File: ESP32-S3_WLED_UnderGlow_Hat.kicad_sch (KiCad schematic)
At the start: 0 parts

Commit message: Update ESP32-S3_WLED_UnderGlow_Hat.kicad_sch
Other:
- title: ESP32-S3_IOHat -> ESP32-S3 WLED UnderGlow Hat
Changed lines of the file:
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@@
 	(paper "A4")
 	(title_block
-		(title "ESP32-S3_IOHat")
+		(title "ESP32-S3 WLED UnderGlow Hat")
 		(date "2026-01-03")
 		(rev "C")

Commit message: Updated Net Names for FSPI and I2S nets
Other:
- sheet IO_Board ports: added FSPI_{CLK}, FSPI_{HD}, FSPI_{MISO}, FSPI_{MOSI}, FSPI_{WP}, I^{2}S_{MCLK}, I^{2}S_{SCK}, I^{2}S_{SD}, I^{2}S_{WS}, ~{FSPI_{CS0}}; removed FSPIHD, FSPIWP, MCLK, MISO, MOSI, SCK, SCLK, SD, WS, ~{FSPICS}
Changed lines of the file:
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@@
 			)
 		)
-		(pin "FSPIHD" bidirectional
+		(pin "FSPI_{HD}" bidirectional
 			(at 109.22 91.44 90)
 			(effects
@@
 			)
 		)
-		(pin "~{FSPICS}" bidirectional
+		(pin "~{FSPI_{CS0}}" bidirectional
 			(at 111.76 91.44 90)
 			(effects
@@
 			)
 		)
-		(pin "MOSI" bidirectional
+		(pin "FSPI_{MOSI}" bidirectional
 			(at 114.3 91.44 90)
 			(effects
@@
 			)
 		)
-		(pin "SCLK" bidirectional
+		(pin "FSPI_{CLK}" bidirectional
 			(at 116.84 91.44 90)
 			(effects
@@
 			)
 		)
-		(pin "MISO" bidirectional
+		(pin "FSPI_{MISO}" bidirectional
 			(at 119.38 91.44 90)
 			(effects
@@
 			)
 		)
-		(pin "FSPIWP" bidirectional
+		(pin "FSPI_{WP}" bidirectional
 			(at 121.92 91.44 90)
 			(effects
@@
 			)
 		)
-		(pin "SD" bidirectional
+		(pin "I^{2}S_{SD}" bidirectional
 			(at 137.16 91.44 90)
 			(effects
@@
 			)
 		)
-		(pin "MCLK" bidirectional
+		(pin "I^{2}S_{MCLK}" bidirectional
 			(at 142.24 91.44 90)
 			(effects
@@
 			)
 		)
-		(pin "SCK" bidirectional
+		(pin "I^{2}S_{SCK}" bidirectional
 			(at 165.1 91.44 90)
 			(effects
@@
 			)
 		)
-		(pin "WS" bidirectional
+		(pin "I^{2}S_{WS}" bidirectional
 			(at 167.64 91.44 90)
 			(effects

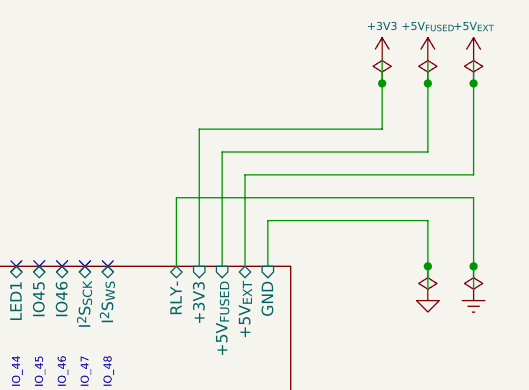
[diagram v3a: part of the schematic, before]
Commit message: schematic updated with new ESP32-S3_D1_Pico symbol
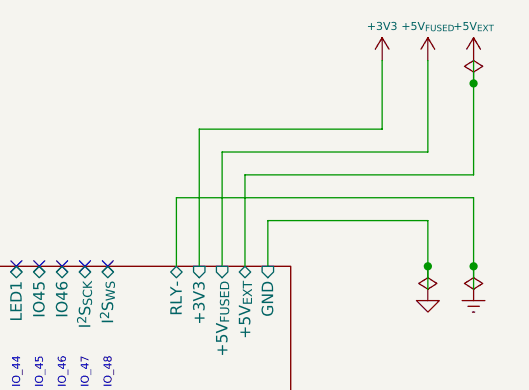
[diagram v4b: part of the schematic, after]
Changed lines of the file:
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@@
-	)
-	(junction
-		(at 198.12 71.12)
-		(diameter 0)
-		(color 0 0 0 0)
 	)
 	(junction
@@
 		(color 0 0 0 0)
 	)
-	(junction
-		(at 203.2 71.12)
-		(diameter 0)
-		(color 0 0 0 0)
-	)
 	(no_connect
 		(at 119.38 91.44)
@@
 	(wire
 		(pts
-			(xy 203.2 68.58) (xy 203.2 71.12)
-		)
-		(stroke
-			(width 0)
-			(type default)
-		)
-	)
-	(wire
-		(pts
 			(xy 180.34 78.74) (xy 203.2 78.74)
 		)
@@
 	(wire
 		(pts
-			(xy 198.12 71.12) (xy 198.12 76.2)
+			(xy 198.12 68.58) (xy 198.12 76.2)
 		)
 		(stroke
@@
 	(wire
 		(pts
-			(xy 203.2 71.12) (xy 203.2 78.74)
+			(xy 203.2 68.58) (xy 203.2 78.74)
 		)
 		(stroke
@@
 		(pts
 			(xy 175.26 83.82) (xy 208.28 83.82)
-		)
-		(stroke
-			(width 0)
-			(type default)
-		)
-	)
-	(wire
-		(pts
-			(xy 198.12 68.58) (xy 198.12 71.12)
 		)
 		(stroke
@@
 	(symbol
 		(lib_id "power:PWR_FLAG")
-		(at 203.2 71.12 0)
-		(unit 1)
-		(exclude_from_sim no)
-		(in_bom yes)
-		(on_board yes)
-		(dnp no)
-		(fields_autoplaced yes)
-		(property "Reference" "#FLG01"
-			(at 203.2 69.215 0)
-			(effects
-				(font
-					(size 0.889 0.889)
-				)
-				(hide yes)
-			)
-		)
-		(property "Value" "+5V_{FUSED}"
-			(at 203.2 66.04 0)
-			(effects
-				(font
-					(size 0.889 0.889)
-				)
-				(hide yes)
-			)
-		)
-		(property "Footprint" ""
-			(at 203.2 71.12 0)
-			(effects
-				(font
-					(size 1.27 1.27)
-				)
-				(hide yes)
-			)
-		)
-		(property "Datasheet" "~"
-			(at 203.2 71.12 0)
-			(effects
-				(font
-					(size 1.27 1.27)
-				)
-				(hide yes)
-			)
-		)
-		(property "Description" "Special symbol for telling ERC where power comes from"
-			(at 203.2 71.12 0)
-			(effects
-				(font
-					(size 1.27 1.27)
-				)
-				(hide yes)
-			)
-		)
-		(pin "1"
-		)
-		(instances
-			(project "ESP32-S3_WLED_UnderGlow_Hat"
-				(path "/67f7b1e1-e87f-421a-8424-bb26889ab157"
-					(reference "#FLG01")
-					(unit 1)
-				)
-			)
-		)
-	)
-	(symbol
-		(lib_id "power:PWR_FLAG")
 		(at 208.28 71.12 0)
 		(unit 1)
@@
 					(unit 1)
 				)
-			)
-		)
-	)
-	(symbol
-		(lib_id "power:PWR_FLAG")
-		(at 198.12 71.12 0)
-		(unit 1)
-		(exclude_from_sim no)
-		(in_bom yes)
-		(on_board yes)
-		(dnp no)
-		(fields_autoplaced yes)
-		(property "Reference" "#FLG0103"
-			(at 198.12 69.215 0)
-			(effects
-				(font
-					(size 0.889 0.889)
-				)
-				(hide yes)
-			)
-		)
-		(property "Value" "+3V3"
-			(at 198.12 66.04 0)
-			(effects
-				(font
-					(size 0.889 0.889)
-				)
-				(hide yes)
-			)
-		)
-		(property "Footprint" ""
-			(at 198.12 71.12 0)
-			(effects
-				(font
-					(size 1.27 1.27)
-				)
-				(hide yes)
-			)
-		)
-		(property "Datasheet" "~"
-			(at 198.12 71.12 0)
-			(effects
-				(font
-					(size 1.27 1.27)
-				)
-				(hide yes)
-			)
-		)
-		(property "Description" "Special symbol for telling ERC where power comes from"
-			(at 198.12 71.12 0)
-			(effects
-				(font
-					(size 1.27 1.27)
-				)
-				(hide yes)
-			)
-		)
-		(pin "1"
-		)
-		(instances
-			(project "ESP32-S3_WLED_UnderGlow_Hat"
-				(path "/67f7b1e1-e87f-421a-8424-bb26889ab157"
-					(reference "#FLG0103")
-					(unit 1)
-				)

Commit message: JLCPCB: W2026061412450502 2026-06-14 PCB: Y62-5297522A PCBA: SMT026061460215-5297522A
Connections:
- no-connect marks 32 -> 27
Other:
- sheet IO_Board ports: added none; removed +5V_{EXT}, IO00, IO01, IO03, IO45, IO46
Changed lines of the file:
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@@
 		(color 0 0 0 0)
 	)
-	(junction
-		(at 208.28 71.12)
-		(diameter 0)
-		(color 0 0 0 0)
-	)
 	(no_connect
 		(at 119.38 91.44)
@@
 	)
 	(no_connect
-		(at 81.28 101.6)
-	)
-	(no_connect
 		(at 114.3 91.44)
 	)
@@
 	)
 	(no_connect
-		(at 81.28 106.68)
-	)
-	(no_connect
 		(at 129.54 91.44)
 	)
@@
 	)
 	(no_connect
-		(at 162.56 91.44)
-	)
-	(no_connect
 		(at 127 91.44)
 	)
@@
 	)
 	(no_connect
-		(at 160.02 91.44)
-	)
-	(no_connect
 		(at 157.48 91.44)
 	)
@@
 		(at 134.62 91.44)
 	)
-	(no_connect
-		(at 81.28 109.22)
-	)
-	(wire
-		(pts
-			(xy 208.28 71.12) (xy 208.28 81.28)
-		)
-		(stroke
-			(width 0)
-			(type default)
-		)
-	)
 	(wire
 		(pts
@@
 	(wire
 		(pts
-			(xy 182.88 81.28) (xy 182.88 91.44)
-		)
-		(stroke
-			(width 0)
-			(type default)
-		)
-	)
-	(wire
-		(pts
 			(xy 198.12 68.58) (xy 198.12 76.2)
 		)
@@
 	(wire
 		(pts
-			(xy 208.28 68.58) (xy 208.28 71.12)
-		)
-		(stroke
-			(width 0)
-			(type default)
-		)
-	)
-	(wire
-		(pts
 			(xy 203.2 68.58) (xy 203.2 78.74)
 		)
@@
 		(pts
 			(xy 175.26 83.82) (xy 208.28 83.82)
-		)
-		(stroke
-			(width 0)
-			(type default)
-		)
-	)
-	(wire
-		(pts
-			(xy 208.28 81.28) (xy 182.88 81.28)
 		)
 		(stroke
@@
 	)
 	(symbol
-		(lib_id "power:PWR_FLAG")
-		(at 208.28 71.12 0)
-		(unit 1)
-		(exclude_from_sim no)
-		(in_bom yes)
-		(on_board yes)
-		(dnp no)
-		(fields_autoplaced yes)
-		(property "Reference" "#FLG0104"
-			(at 208.28 69.215 0)
-			(effects
-				(font
-					(size 0.889 0.889)
-				)
-				(hide yes)
-			)
-		)
-		(property "Value" "+5V_{EXT}"
-			(at 208.28 66.04 0)
-			(effects
-				(font
-					(size 0.889 0.889)
-				)
-				(hide yes)
-			)
-		)
-		(property "Footprint" ""
-			(at 208.28 71.12 0)
-			(effects
-				(font
-					(size 1.27 1.27)
-				)
-				(hide yes)
-			)
-		)
-		(property "Datasheet" "~"
-			(at 208.28 71.12 0)
-			(effects
-				(font
-					(size 1.27 1.27)
-				)
-				(hide yes)
-			)
-		)
-		(property "Description" "Special symbol for telling ERC where power comes from"
-			(at 208.28 71.12 0)
-			(effects
-				(font
-					(size 1.27 1.27)
-				)
-				(hide yes)
-			)
-		)
-		(pin "1"
-		)
-		(instances
-			(project "ESP32-S3_WLED_UnderGlow_Hat"
-				(path "/67f7b1e1-e87f-421a-8424-bb26889ab157"
-					(reference "#FLG0104")
-					(unit 1)
-				)
-			)
-		)
-	)
-	(symbol
 		(lib_id "power:GND")
 		(at 203.2 93.98 0)
@@
 		)
 	)
-	(symbol
-		(lib_id "power:+3V3")
-		(at 208.28 68.58 0)
-		(unit 1)
-		(exclude_from_sim no)
-		(in_bom yes)
-		(on_board yes)
-		(dnp no)
-		(property "Reference" "#PWR0104"
-			(at 208.28 72.39 0)
-			(effects
-				(font
-					(size 0.889 0.889)
-				)
-				(hide yes)
-			)
-		)
-		(property "Value" "+5V_{EXT}"
-			(at 208.28 64.77 0)
-			(effects
-				(font
-					(size 0.889 0.889)
-				)
-			)
-		)
-		(property "Footprint" ""
-			(at 208.28 68.58 0)
-			(effects
-				(font
-					(size 1.27 1.27)
-				)
-				(hide yes)
-			)
-		)
-		(property "Datasheet" ""
-			(at 208.28 68.58 0)
-			(effects
-				(font
-					(size 1.27 1.27)
-				)
-				(hide yes)
-			)
-		)
-		(property "Description" "Power symbol creates a global label with name \"+3V3\""
-			(at 208.28 68.58 0)
-			(effects
-				(font
-					(size 1.27 1.27)
-				)
-				(hide yes)
-			)
-		)
-		(pin "1"
-		)
-		(instances
-			(project "ESP32-S3_WLED_UnderGlow_Hat"
-				(path "/67f7b1e1-e87f-421a-8424-bb26889ab157"
-					(reference "#PWR0104")
-					(unit 1)
-				)
-			)
-		)
-	)
 	(sheet
 		(at 81.28 91.44)
@@
 			)
 		)
-		(pin "IO00" bidirectional
-			(at 81.28 109.22 180)
-			(effects
-				(font
-					(size 1.27 1.27)
-				)
-				(justify left)
-			)
-		)
-		(pin "IO01" bidirectional
-			(at 81.28 106.68 180)
-			(effects
-				(font
-					(size 1.27 1.27)
-				)
-				(justify left)
-			)
-		)
 		(pin "WD" bidirectional
 			(at 81.28 104.14 180)
@@
 			)
 		)
-		(pin "IO03" bidirectional
-			(at 81.28 101.6 180)
-			(effects
-				(font
-					(size 1.27 1.27)
-				)
-				(justify left)
-			)
-		)
 		(pin "~{Wake}" bidirectional
 			(at 81.28 99.06 180)
@@
 			)
 		)
-		(pin "IO45" bidirectional
-			(at 160.02 91.44 90)
-			(effects
-				(font
-					(size 1.27 1.27)
-				)
-				(justify right)
-			)
-		)
-		(pin "IO46" bidirectional
-			(at 162.56 91.44 90)
-			(effects
-				(font
-					(size 1.27 1.27)
-				)
-				(justify right)
-			)
-		)
 		(pin "I^{2}S_{SCK}" bidirectional
 			(at 165.1 91.44 90)
@@
 			(effects
 				(font
-					(size 1.27 1.27)
-				)
-				(justify right)
-			)
-		)
-		(pin "+5V_{EXT}" bidirectional
-			(at 182.88 91.44 90)
-			(effects
-				(font
